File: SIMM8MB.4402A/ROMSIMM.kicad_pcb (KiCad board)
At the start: 4 copper layers, 97.8 x 25 mm, 34 parts, among them J1 ROM, U1 MX29LV320, U10 74AHC245, U11 LD1117S33, U2 MX29LV320, U3 74AHC245, U4 74AHC245, U5 74AHC245, U6 74AHC245, U7 74AHC245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

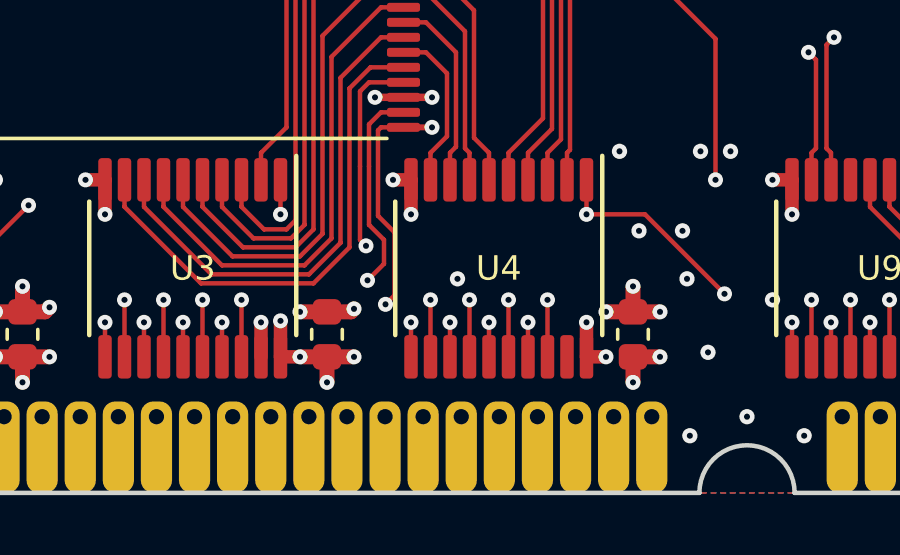
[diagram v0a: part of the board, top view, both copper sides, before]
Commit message: Switched GW number of 8MB simm to 4402A
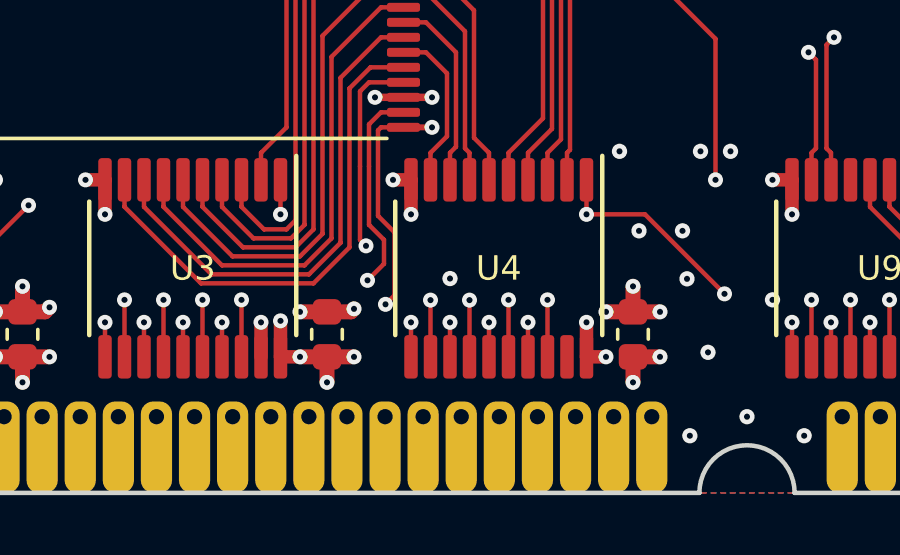
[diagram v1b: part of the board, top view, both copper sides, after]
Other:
- board text added: "4402A"
- board text removed: "4401B"
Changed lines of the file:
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@@
       (net 7 GND) (zone_connect 2))
   )
-  (gr_text 4401B (at 146.833286 114.3) (layer B.SilkS)
+  (gr_text 4402A (at 146.833286 114.3) (layer B.SilkS)
     (effects (font (size 1.5 1.5) (thickness 0.3)) (justify left mirror))
   )
@@
   (via (at 118.5 118.9) (size 0.508) (drill 0.2) (layers F.Cu B.Cu) (net 7))
   (via (at 118.65 120.5) (size 0.508) (drill 0.2) (layers F.Cu B.Cu) (net 7))
-  (via (at 111 120.5) (size 0.508) (drill 0.2) (layers F.Cu B.Cu) (net 7))
+  (via (at 110.75 120.49) (size 0.508) (drill 0.2) (layers F.Cu B.Cu) (net 7))
   (segment (start 106.65 121.6) (end 107.45 121.6) (width 0.5) (layer F.Cu) (net 7))
   (segment (start 107.45 121.6) (end 107.55 121.5) (width 0.5) (layer F.Cu) (net 7))
@@
   (segment (start 109.1 122.3) (end 109.45 121.95) (width 0.15) (layer In2.Cu) (net 23))
   (segment (start 105.85 122.3) (end 109.1 122.3) (width 0.15) (layer In2.Cu) (net 23))
-  (via (at 110.1 121.2) (size 0.5) (drill 0.2) (layers F.Cu B.Cu) (net 24))
-  (segment (start 110.1 123.1) (end 110.1 121.2) (width 0.15) (layer F.Cu) (net 24))
-  (segment (start 106.045 125.095) (end 106.045 123.855) (width 0.15) (layer In2.Cu) (net 24))
-  (segment (start 106.045 123.855) (end 107.3 122.6) (width 0.15) (layer In2.Cu) (net 24))
-  (segment (start 107.3 122.6) (end 109.5 122.6) (width 0.15) (layer In2.Cu) (net 24))
-  (segment (start 109.5 122.6) (end 110.1 122) (width 0.15) (layer In2.Cu) (net 24))
-  (segment (start 110.1 121.2) (end 110.1 122) (width 0.15) (layer In2.Cu) (net 24))
+  (segment (start 106.045 123.855) (end 106.045 125.095) (width 0.15) (layer In2.Cu) (net 24))
+  (segment (start 110.1 122) (end 109.5 122.6) (width 0.15) (layer In2.Cu) (net 24))
+  (segment (start 107.3 122.6) (end 106.045 123.855) (width 0.15) (layer In2.Cu) (net 24))
+  (segment (start 109.5 122.6) (end 107.3 122.6) (width 0.15) (layer In2.Cu) (net 24))
+  (via (at 110.1 121.21) (size 0.5) (drill 0.2) (layers F.Cu B.Cu) (net 24))
+  (segment (start 110.1 123.1) (end 110.1 121.21) (width 0.15) (layer F.Cu) (net 24))
+  (segment (start 110.1 121.21) (end 110.1 122) (width 0.15) (layer In2.Cu) (net 24))
   (via (at 110.75 121.95) (size 0.5) (drill 0.2) (layers F.Cu B.Cu) (net 25))
   (segment (start 110.75 123.1) (end 110.75 121.95) (width 0.15) (layer F.Cu) (net 25))
@@
   (segment (start 107.315 124.035) (end 107.315 125.095) (width 0.15) (layer In2.Cu) (net 25))
   (segment (start 108.45 122.9) (end 107.315 124.035) (width 0.15) (layer In2.Cu) (net 25))
-  (segment (start 111.4 123.1) (end 111.4 121.2) (width 0.15) (layer F.Cu) (net 26))
-  (via (at 111.4 121.2) (size 0.5) (drill 0.2) (layers F.Cu B.Cu) (net 26))
-  (segment (start 111.4 122) (end 111.4 121.2) (width 0.15) (layer In2.Cu) (net 26))
-  (segment (start 109.8 123.2) (end 110.55 122.45) (width 0.15) (layer In2.Cu) (net 26))
-  (segment (start 109.1 123.2) (end 109.8 123.2) (width 0.15) (layer In2.Cu) (net 26))
-  (segment (start 108.585 123.715) (end 109.1 123.2) (width 0.15) (layer In2.Cu) (net 26))
-  (segment (start 110.55 122.45) (end 110.95 122.45) (width 0.15) (layer In2.Cu) (net 26))
-  (segment (start 108.585 125.095) (end 108.585 123.715) (width 0.15) (layer In2.Cu) (net 26))
-  (segment (start 110.95 122.45) (end 111.4 122) (width 0.15) (layer In2.Cu) (net 26))
+  (segment (start 109.1 123.2) (end 108.585 123.715) (width 0.15) (layer In2.Cu) (net 26))
+  (segment (start 109.8 123.2) (end 109.1 123.2) (width 0.15) (layer In2.Cu) (net 26))
+  (segment (start 111.4 122) (end 110.95 122.45) (width 0.15) (layer In2.Cu) (net 26))
+  (segment (start 108.585 123.715) (end 108.585 125.095) (width 0.15) (layer In2.Cu) (net 26))
+  (segment (start 110.95 122.45) (end 110.55 122.45) (width 0.15) (layer In2.Cu) (net 26))
+  (segment (start 110.55 122.45) (end 109.8 123.2) (width 0.15) (layer In2.Cu) (net 26))
+  (via (at 111.4 121.21) (size 0.5) (drill 0.2) (layers F.Cu B.Cu) (net 26))
+  (segment (start 111.4 121.21) (end 111.4 122) (width 0.15) (layer In2.Cu) (net 26))
+  (segment (start 111.4 123.1) (end 111.4 121.21) (width 0.15) (layer F.Cu) (net 26))
   (segment (start 112.05 123.1) (end 112.05 121.95) (width 0.15) (layer F.Cu) (net 27))
   (via (at 112.05 121.95) (size 0.5) (drill 0.2) (layers F.Cu B.Cu) (net 27))
@@
   (segment (start 80.9 117.2) (end 80.9 116.05) (width 0.15) (layer F.Cu) (net 99))
   (via (at 108.6 121.35) (size 0.5) (drill 0.2) (layers F.Cu B.Cu) (net 99))
-  (segment (start 108.9 121.05) (end 108.6 121.35) (width 0.15) (layer F.Cu) (net 99))
-  (segment (start 109.2 115.45) (end 108.45 115.45) (width 0.15) (layer F.Cu) (net 99))
-  (segment (start 108.9 118.95) (end 108.9 121.05) (width 0.15) (layer F.Cu) (net 99))
-  (segment (start 108.35 118.4) (end 108.9 118.95) (width 0.15) (layer F.Cu) (net 99))
-  (segment (start 108.35 115.55) (end 108.35 118.4) (width 0.15) (layer F.Cu) (net 99))
-  (segment (start 108.45 115.45) (end 108.35 115.55) (width 0.15) (layer F.Cu) (net 99))
   (via (at 110.15 115.45) (size 0.5) (drill 0.2) (layers F.Cu B.Cu) (net 99))
   (segment (start 109.2 115.45) (end 110.15 115.45) (width 0.2) (layer F.Cu) (net 99))
@@
   (segment (start 151.2 115.45) (end 150.95 115.7) (width 0.15) (layer F.Cu) (net 99))
   (segment (start 151.99 115.45) (end 151.2 115.45) (width 0.15) (layer F.Cu) (net 99))
-  (segment (start 109.2 114.95) (end 108.45 114.95) (width 0.15) (layer F.Cu) (net 102))
-  (segment (start 108.45 114.95) (end 108.05 115.35) (width 0.15) (layer F.Cu) (net 102))
-  (segment (start 108.05 115.35) (end 108.05 116.75) (width 0.15) (layer F.Cu) (net 102))
-  (segment (start 108.05 116.75) (end 108.05 118.7) (width 0.15) (layer F.Cu) (net 102))
-  (segment (start 108.05 118.7) (end 108.55 119.2) (width 0.15) (layer F.Cu) (net 102))
-  (segment (start 108.55 119.2) (end 108.55 120) (width 0.15) (layer F.Cu) (net 102))
+  (segment (start 108.9 118.95) (end 108.9 121.05) (width 0.15) (layer F.Cu) (net 99))
+  (segment (start 108.35 118.4) (end 108.9 118.95) (width 0.15) (layer F.Cu) (net 99))
+  (segment (start 108.35 115.55) (end 108.35 118.4) (width 0.15) (layer F.Cu) (net 99))
+  (segment (start 108.9 121.05) (end 108.6 121.35) (width 0.15) (layer F.Cu) (net 99))
+  (segment (start 108.45 115.45) (end 108.35 115.55) (width 0.15) (layer F.Cu) (net 99))
+  (segment (start 109.2 115.45) (end 108.45 115.45) (width 0.15) (layer F.Cu) (net 99))
   (via (at 108 120.55) (size 0.5) (drill 0.2) (layers F.Cu B.Cu) (net 102))
-  (segment (start 108.55 120) (end 108 120.55) (width 0.15) (layer F.Cu) (net 102))
   (via (at 91.7 118.35) (size 0.5) (drill 0.2) (layers F.Cu B.Cu) (net 102))
   (segment (start 91.7 117.2) (end 91.7 118.35) (width 0.15) (layer F.Cu) (net 102))
@@
   (segment (start 151.99 114.95) (end 151.05 114.95) (width 0.15) (layer F.Cu) (net 102))
   (via (at 151.05 114.95) (size 0.5) (drill 0.2) (layers F.Cu B.Cu) (net 102))
+  (segment (start 108.05 116.75) (end 108.05 118.7) (width 0.15) (layer F.Cu) (net 102))
+  (segment (start 108.05 118.7) (end 108.55 119.2) (width 0.15) (layer F.Cu) (net 102))
+  (segment (start 108.55 120) (end 108 120.55) (width 0.15) (layer F.Cu) (net 102))
+  (segment (start 108.05 115.35) (end 108.05 116.75) (width 0.15) (layer F.Cu) (net 102))
+  (segment (start 108.45 114.95) (end 108.05 115.35) (width 0.15) (layer F.Cu) (net 102))
+  (segment (start 108.55 119.2) (end 108.55 120) (width 0.15) (layer F.Cu) (net 102))
+  (segment (start 109.2 114.95) (end 108.45 114.95) (width 0.15) (layer F.Cu) (net 102))
   (segment (start 109.2 113.95) (end 108.05 113.95) (width 0.15) (layer F.Cu) (net 103))
   (segment (start 108.05 113.95) (end 107.75 114.25) (width 0.15) (layer F.Cu) (net 103))
